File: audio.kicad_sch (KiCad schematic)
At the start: 5 parts, among them U2 MAX98357A

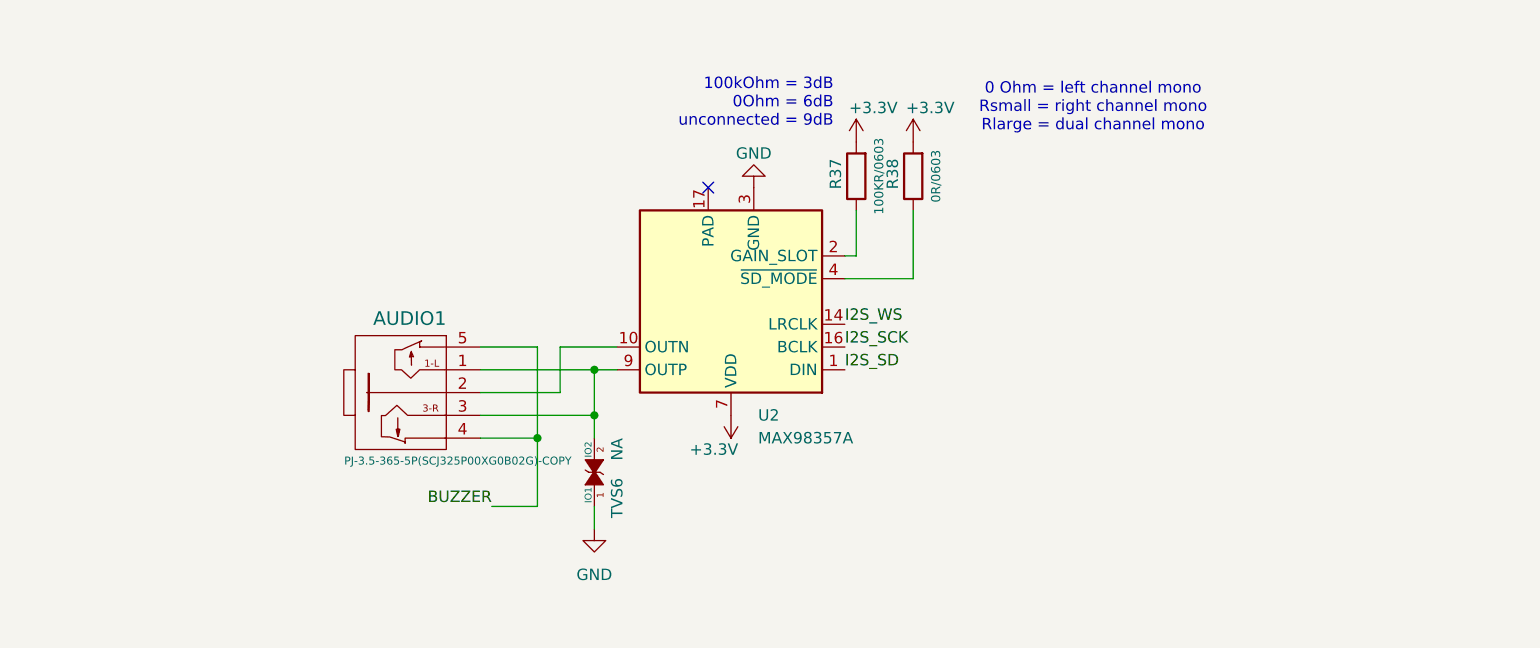
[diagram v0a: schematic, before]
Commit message: schematics finished, pcb routing 80%
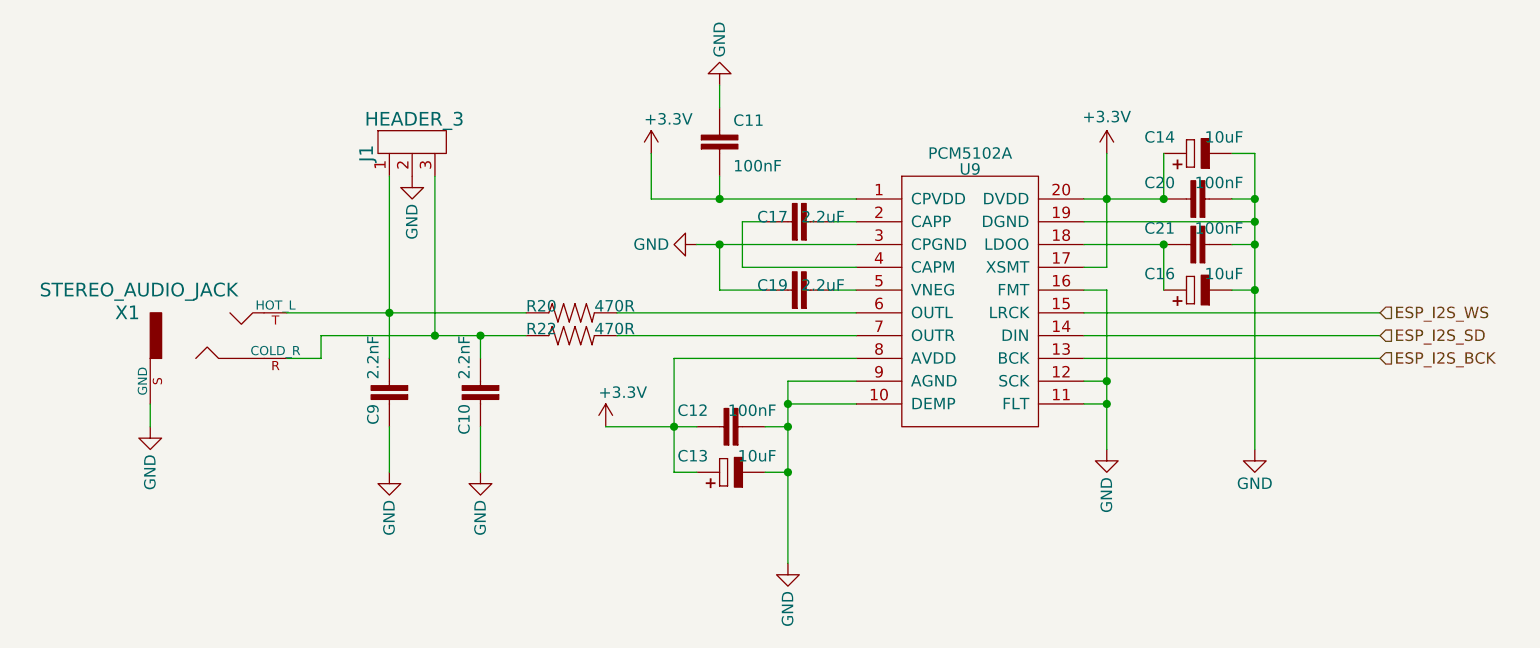
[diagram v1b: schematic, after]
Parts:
- removed AUDIO1: PJ-3.5-365-5P(SCJ325P00XG0B02G)-COPY, OLIMEX_Connectors-FP:SCJ325P00XG0B02G, symbol AgonLight2_Rev_B:AUDIO_JACK(SCJ325P00XG0B02G)
- removed R37: 100KR/0603, OLIMEX_RLC-FP:R_0603_5MIL_DWS, symbol AgonLight2_Rev_B:R
- removed R38: 0R/0603, OLIMEX_RLC-FP:R_0603_5MIL_DWS, symbol AgonLight2_Rev_B:R
- removed TVS6: NA, OLIMEX_Diodes-FP:D_0402_5MIL_DWS, symbol AgonLight2_Rev_B:GG0402052R542P
- removed U2: MAX98357A, Package_DFN_QFN:TQFN-16-1EP_3x3mm_P0.5mm_EP1.23x1.23mm, symbol Audio:MAX98357A
- added C10, C9: 2.2nF, HexAgonFootprintsLibrary:C_0603_5MIL_DWS, symbol pidac_5102A-rescue:C_EU
- added C11, C12, C20, C21: 100nF, HexAgonFootprintsLibrary:C_0603_5MIL_DWS, symbol pidac_5102A-rescue:C_EU
- added C13, C14, C16: 10uF, HexAgonFootprintsLibrary:C_0603_5MIL_DWS, symbol pidac_5102A-rescue:CPOL_EU
- added C17, C19: 2.2uF, HexAgonFootprintsLibrary:C_0603_5MIL_DWS, symbol pidac_5102A-rescue:C_EU
- added J1: HEADER_3, Connector_PinHeader_2.54mm:PinHeader_1x03_P2.54mm_Vertical, symbol pidac_5102A-rescue:HEADER_3
- added R20, R22: 470R, HexAgonFootprintsLibrary:R_0603_5MIL_DWS, symbol pidac_5102A-rescue:R_US
- added U9: PCM5102A, Package_SO:TSSOP-20_4.4x6.5mm_P0.65mm, symbol pidac_5102A-rescue:PCM5102A
- added X1: STEREO_AUDIO_JACK, Connector_Audio:Jack_3.5mm_CUI_SJ-3523-SMT_Horizontal, symbol pidac_5102A-rescue:STEREO_AUDIO_JACK
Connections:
- net +3.3V: now also C11.2, C12.1, C13.1 (+), C14.1 (+), C20.1, U9.1 (CPVDD), U9.17 (XSMT), U9.20 (DVDD), U9.8 (AVDD)
- net GND: now also C10.1, C11.1, C12.2, C13.2 (-), C14.2 (-), C16.2 (-), C19.1, C20.2, C21.2, C9.1, J1.2, U9.10 (DEMP), U9.11 (FLT), U9.12 (SCK), U9.16 (FMT), U9.19 (DGND), U9.3 (CPGND), U9.9 (AGND), X1.S (GND)
- new net: C10.2, J1.3, R22.1, X1.R (COLD_R)
- new net: C16.1 (+), C21.1, U9.18 (LDOO)
- new net: C17.2, U9.2 (CAPP)
- new net: C17.1, U9.4 (CAPM)
- new net: C19.2, U9.5 (VNEG)
- new net: R20.2, U9.6 (OUTL)
- new net: R22.2, U9.7 (OUTR)
- new net: C9.2, J1.1, R20.1, X1.T (HOT_L)
- new net ESP_I2S_BCK: U9.13 (BCK)
- new net ESP_I2S_SD: U9.14 (DIN)
- new net ESP_I2S_WS: U9.15 (LRCK)
- no-connect marks 1 -> 0
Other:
- note removed: "0 Ohm = left channel mono Rsmall = right channel mono Rlarge = dual channel mono"
- note removed: "100kOhm = 3dB 0Ohm = 6dB unconnected = 9dB"

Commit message: 1st production and BOM
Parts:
- C10, C9: MfgNumber (none) -> GRM1857U1H222JA44D
- C11, C12, C20, C21: value 100nF -> 0.1uF/6.3V/20%/X5R/C0603; MfgNumber (none) -> GRM188R72A104MA35D
- C13, C14, C16: MfgNumber (none) -> T58MM106M6R3C0500
- C17, C19: MfgNumber (none) -> GRM185R60J225KE26D
- J1: MfgNumber (none) -> 9-146276-0
- R20, R22: MfgNumber (none) -> ESR03EZPJ471
- U9: MfgNumber (none) -> PCM5102APWR
- X1: MfgNumber (none) -> SJ-3523-SMT-TR
